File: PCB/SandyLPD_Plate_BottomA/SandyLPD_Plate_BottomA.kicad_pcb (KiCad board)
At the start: 2 copper layers, 127.4 x 83 mm, 146 parts, among them J1 Conn_02x02_Odd_Even, J2 Conn_01x03, J4 Conn_01x10_Pin, J5 USB_C_Receptacle_USB2.0, J6 USB_C_Receptacle_USB2.0, SW1 BOOT_ALT, SW2 RESET_ALT, SW3 SW_DIP_x04, U1 NCP1117-3.3_SOT223, U3 RP2040, U4 W25Q128JVPIQ, Y1 12MHz

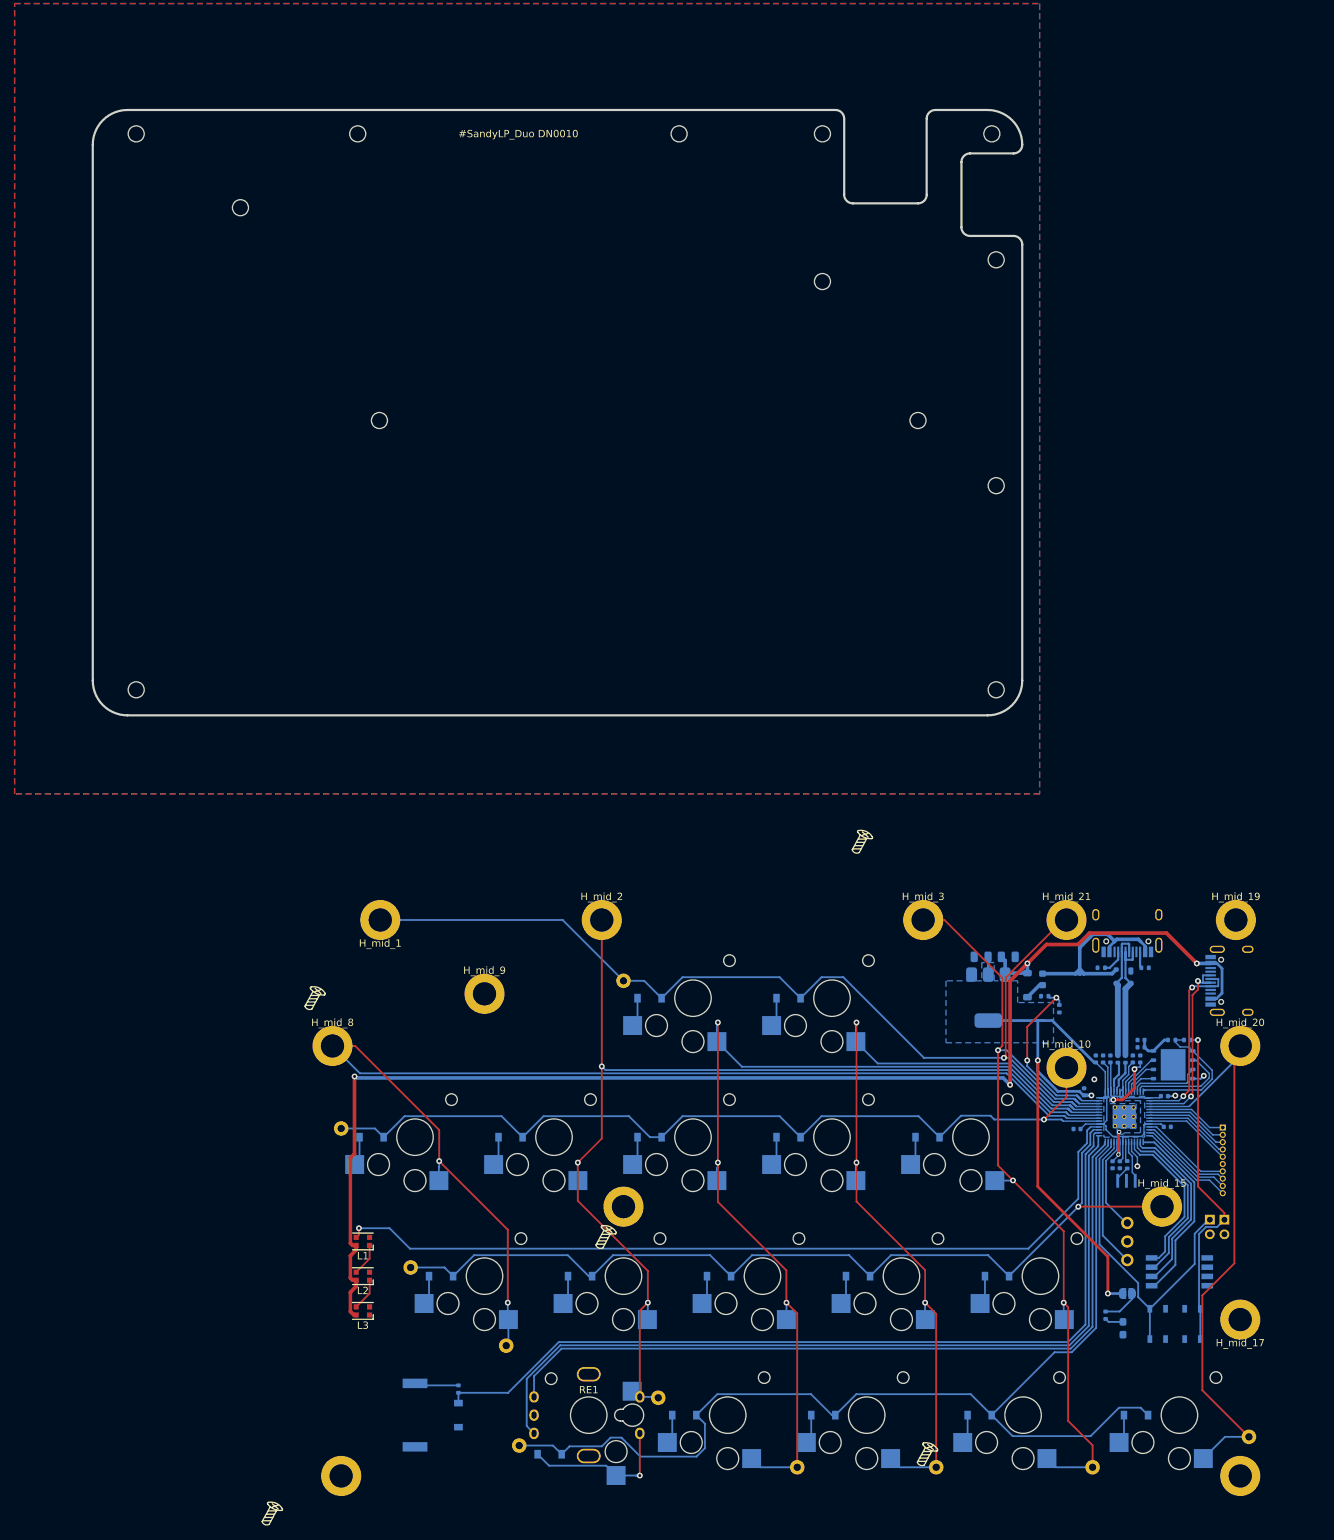
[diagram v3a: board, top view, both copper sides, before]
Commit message: ソケット逃し穴の形状を変更
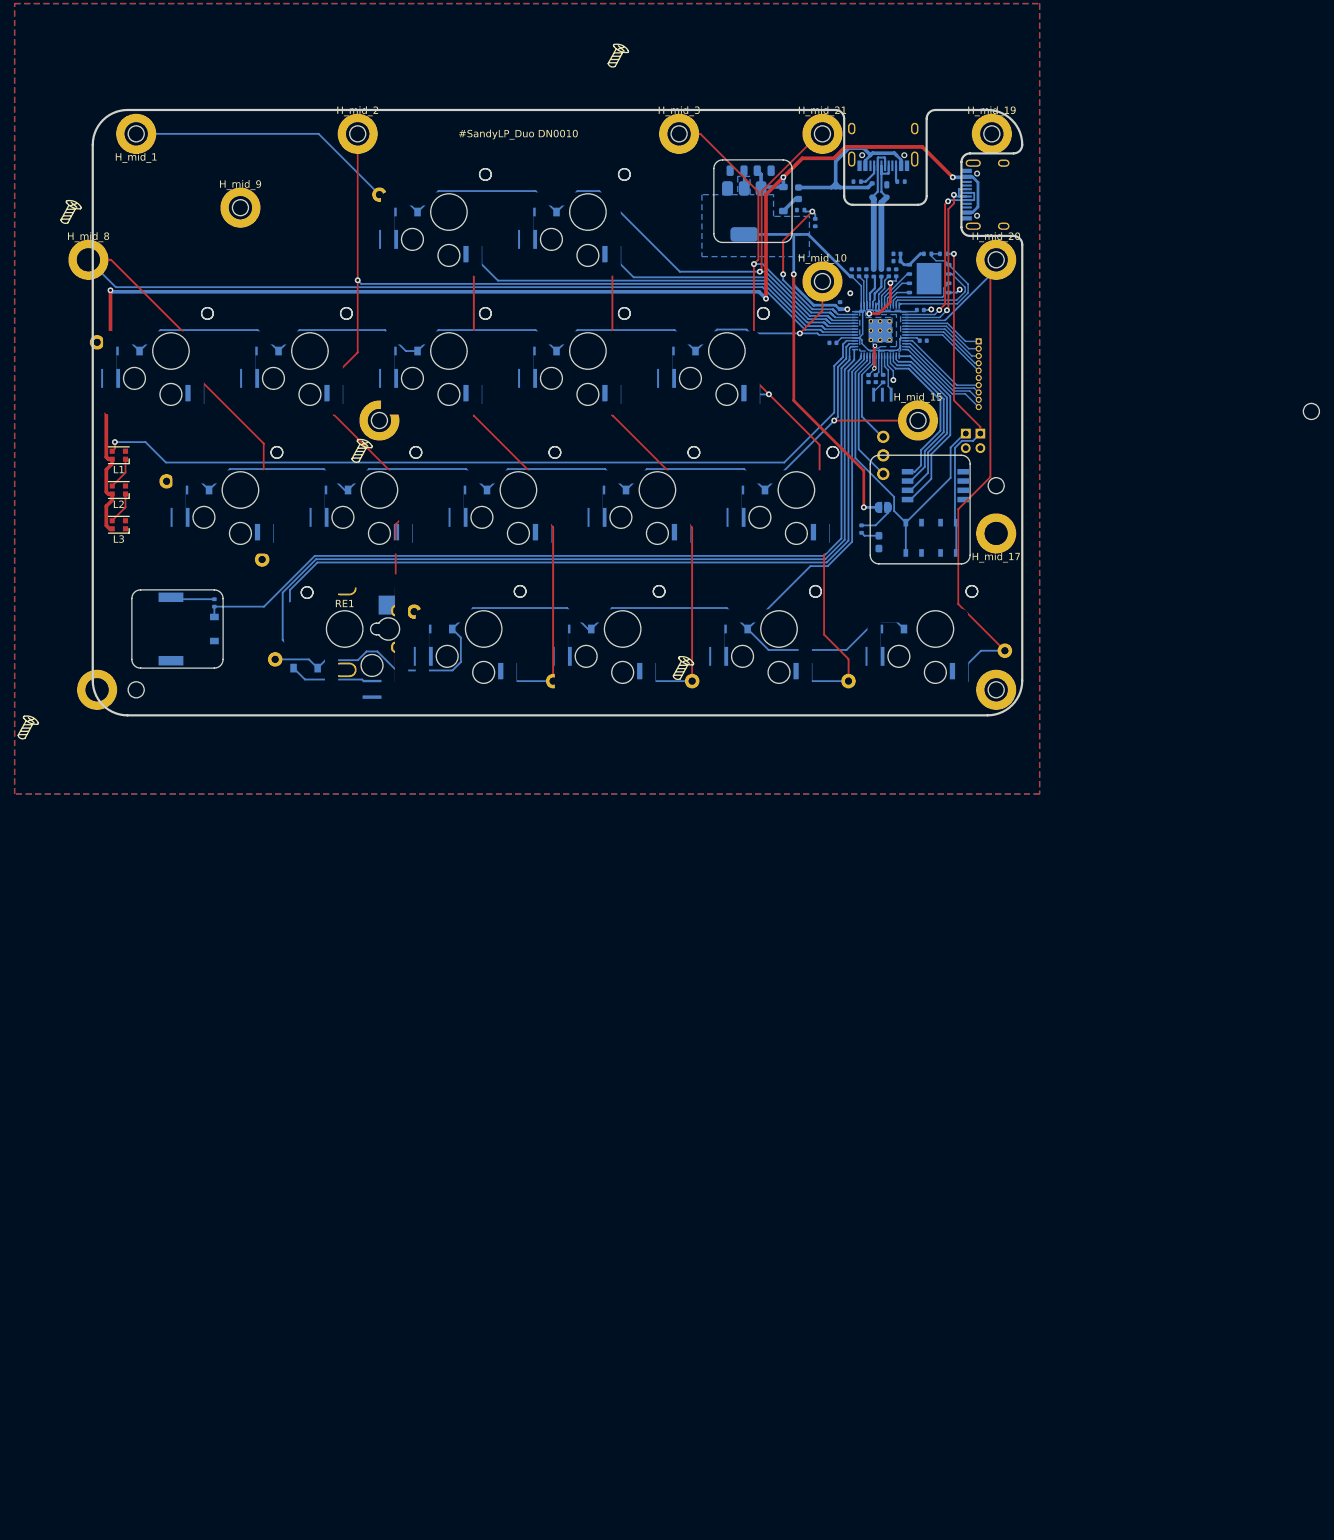
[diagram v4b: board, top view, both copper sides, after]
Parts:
- added H1: MountingHole, locallib:Kailh_socket_ChocV2_cutout_type2, F.Cu at (75.8, 46.1)
- added H10: MountingHole, locallib:Kailh_socket_ChocV2_cutout_type2, F.Cu at (85.4, 84.2)
- added H11: MountingHole, locallib:Kailh_socket_ChocV2_cutout_type2, F.Cu at (104.4, 84.2)
- added H12: MountingHole, locallib:Kailh_socket_ChocV2_cutout_type2, F.Cu at (123.5, 84.2)
- added H13: MountingHole, locallib:Kailh_socket_ChocV2_and_RotaryEncoder_cutout_type2, F.Cu at (61.5, 103.2)
- added H14: MountingHole, locallib:Kailh_socket_ChocV2_cutout_type2, F.Cu at (80.6, 103.2)
- added H15: MountingHole, locallib:Kailh_socket_ChocV2_cutout_type2, F.Cu at (99.6, 103.2)
- added H16: MountingHole, locallib:Kailh_socket_ChocV2_cutout_type2, F.Cu at (121.1, 103.2)
- added H17: MountingHole, locallib:Kailh_socket_ChocV2_cutout_type2, F.Cu at (142.5, 103.2)
- added H2: MountingHole, locallib:Kailh_socket_ChocV2_cutout_type2, F.Cu at (94.9, 46.1)
- added H3: MountingHole, locallib:Kailh_socket_ChocV2_cutout_type2, F.Cu at (37.7, 65.1)
- added H4: MountingHole, locallib:Kailh_socket_ChocV2_cutout_type2, F.Cu at (56.8, 65.1)
- added H5: MountingHole, locallib:Kailh_socket_ChocV2_cutout_type2, F.Cu at (75.8, 65.1)
- added H6: MountingHole, locallib:Kailh_socket_ChocV2_cutout_type2, F.Cu at (94.9, 65.1)
- added H7: MountingHole, locallib:Kailh_socket_ChocV2_cutout_type2, F.Cu at (113.9, 65.1)
- added H8: MountingHole, locallib:Kailh_socket_ChocV2_cutout_type2, F.Cu at (47.3, 84.2)
- added H9: MountingHole, locallib:Kailh_socket_ChocV2_cutout_type2, F.Cu at (66.3, 84.2)
- added H_mid_8: MountingHole, locallib:MountingHole_2.2mm_M2_no_REF, F.Cu at (194.0, 73.4)
- REF**: footprint locallib:SandyLP-Duo_outline_BottomA_with_hole2_narrow_edge -> locallib:SandyLP-Duo_outline_BottomA_narrow_edge
- moved C1 112.8 mm to (119.0, 40.4)
- moved C14 112.8 mm to (133.0, 54.4)
- moved C15 112.8 mm to (132.0, 54.4)
- moved C2 112.8 mm to (115.3, 40.4)
- moved C3 112.8 mm to (137.1, 54.4)
- moved C4 112.8 mm to (133.3, 68.9)
- moved C5 112.8 mm to (136.1, 54.4)
- moved C6 112.8 mm to (134.3, 68.9)
- moved C7 112.8 mm to (129.4, 58.9)
- moved C9 112.8 mm to (131.0, 54.4)
- moved H_btm_1 112.8 mm to (66.3, 74.6)
- moved H_mid_1 112.8 mm to (33.0, 35.3)
- moved H_mid_15 112.8 mm to (140.1, 74.6)
- moved H_mid_17 112.8 mm to (150.8, 90.1)
- moved J2 112.8 mm to (135.4, 76.9)
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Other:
- outline, holes or cut-outs redrawn

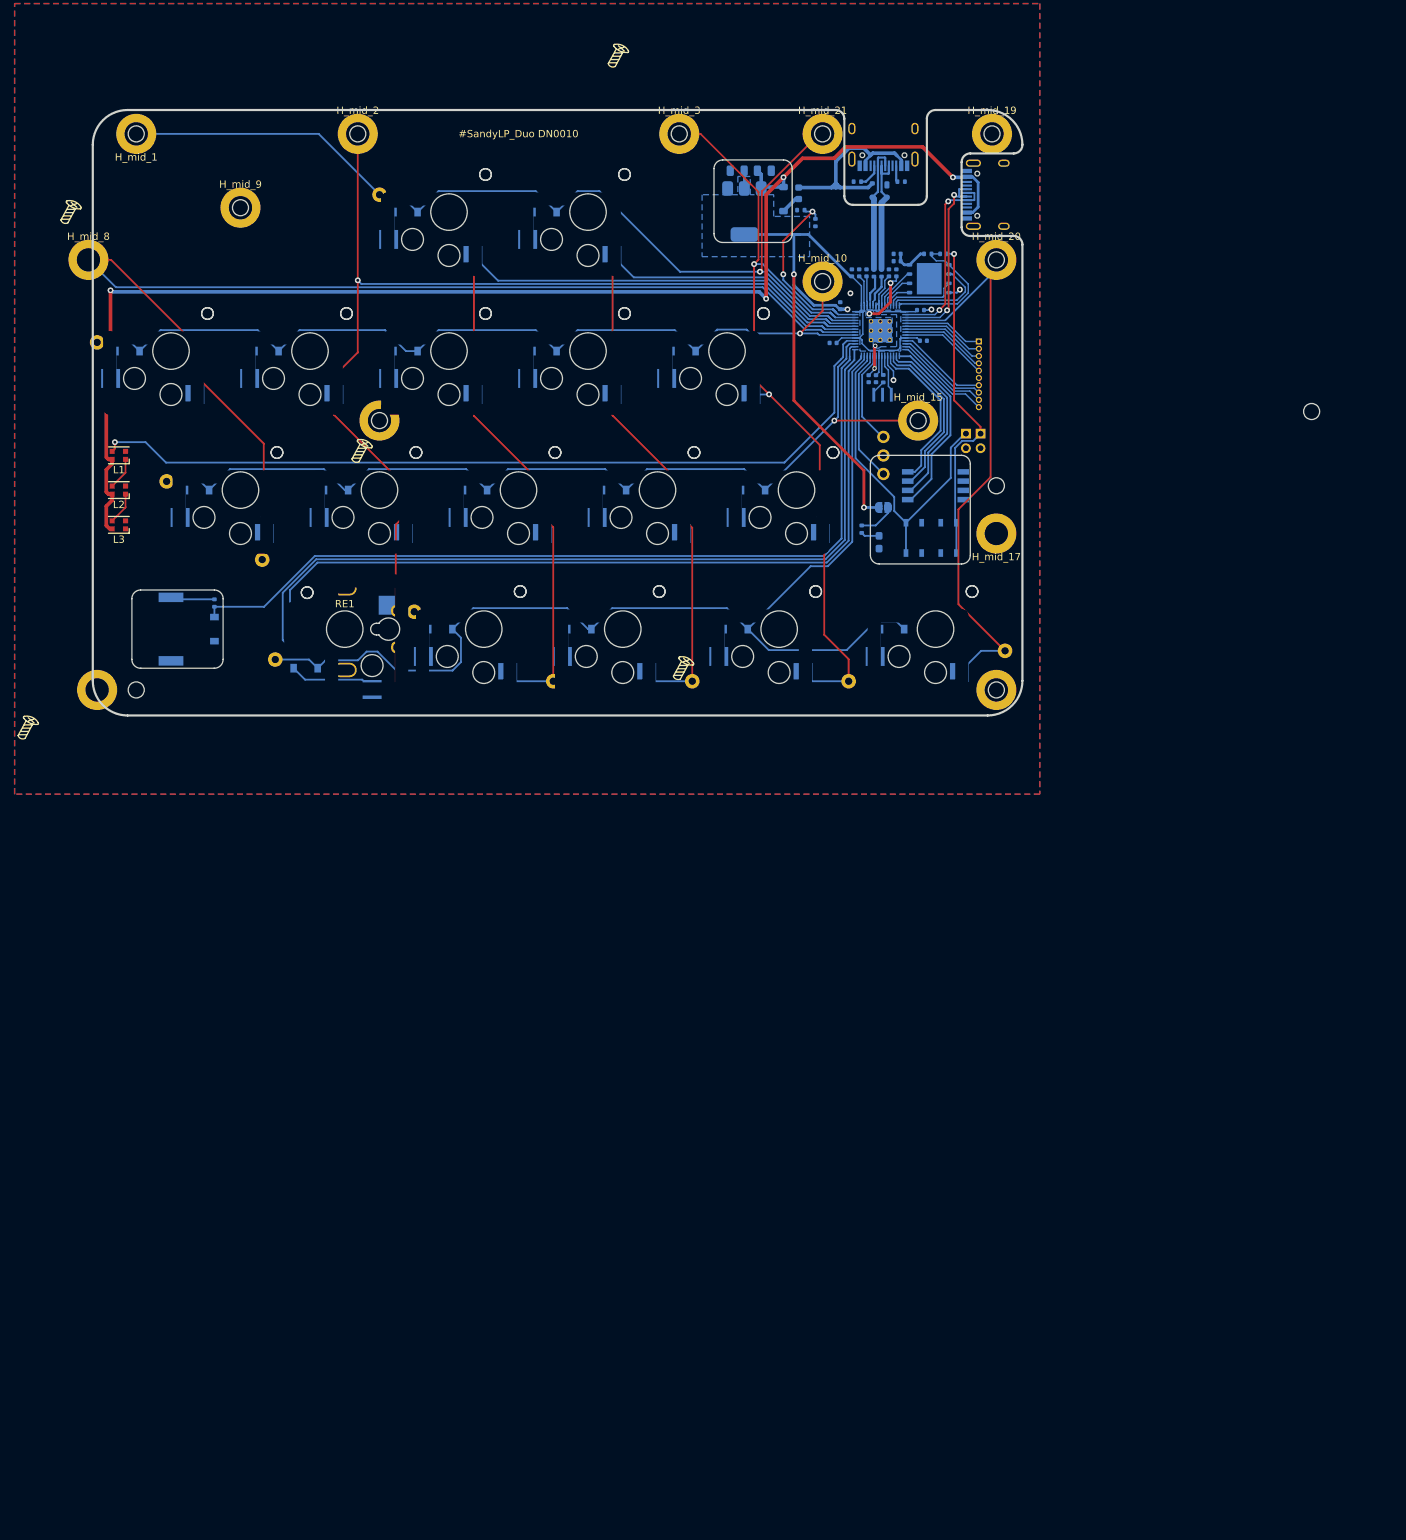
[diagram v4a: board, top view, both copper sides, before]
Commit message: EC11Kサポート廃止（新規設計非推奨のため）
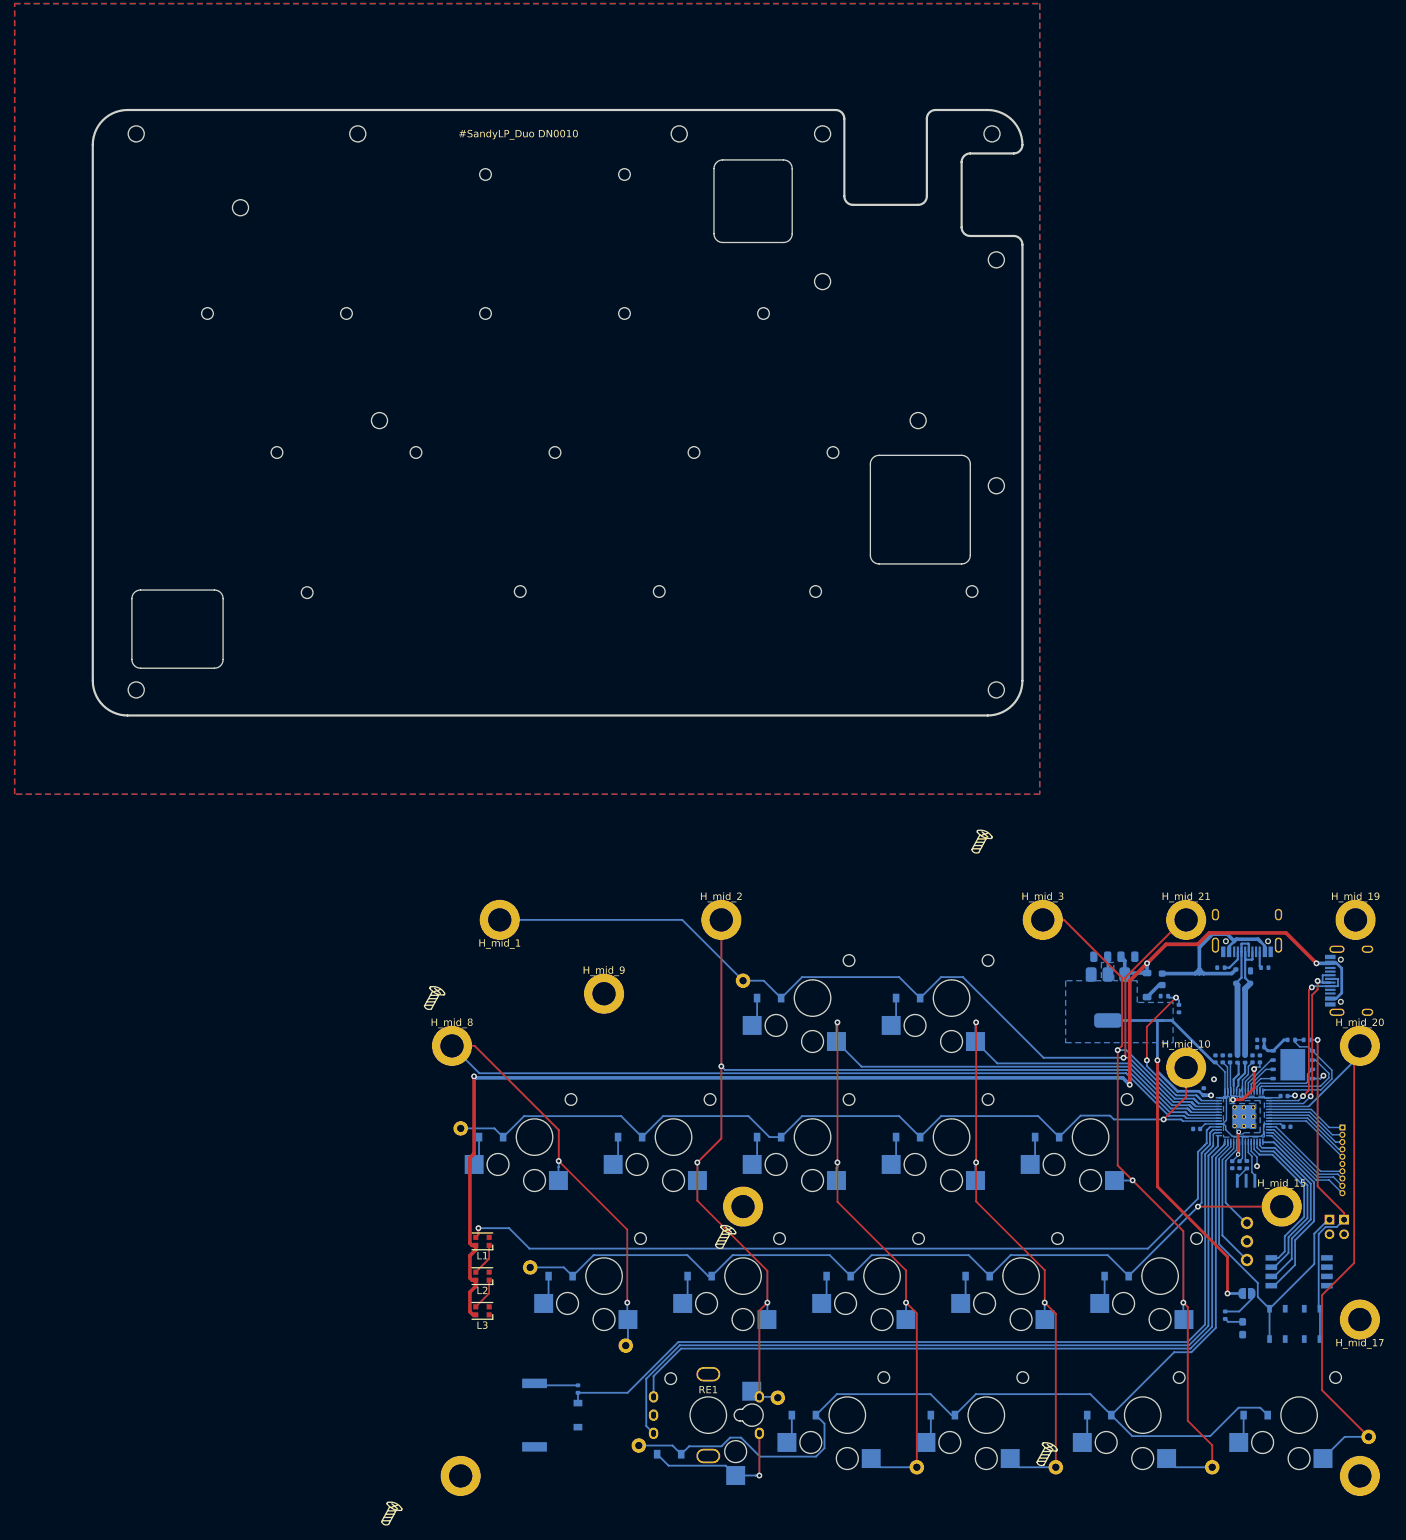
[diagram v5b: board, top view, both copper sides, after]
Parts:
- removed the H_mid_8 at (194.0, 73.4)
- moved C10 118.7 mm to (190.7, 171.4)
- moved C12 118.7 mm to (187.1, 160.5)
- moved C13 118.7 mm to (187.1, 159.5)
- moved D1 118.7 mm to (119.7, 153.8)
- moved D2 118.7 mm to (138.7, 153.8)
- moved D36 118.7 mm to (184.7, 150.8)
- moved D5 118.7 mm to (81.6, 172.8)
- moved D6 118.7 mm to (100.6, 172.8)
- moved D7 118.7 mm to (119.7, 172.8)
- moved D8 118.7 mm to (138.7, 172.8)
- moved D9 118.7 mm to (157.8, 172.8)
- moved H_btm_3 118.7 mm to (77.4, 219.3)
- moved H_btm_4 118.7 mm to (200.7, 219.3)
- moved H_mid_19 118.7 mm to (200.1, 143.1)
- moved H_mid_2 118.7 mm to (113.1, 143.1)
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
